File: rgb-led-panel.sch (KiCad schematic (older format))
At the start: 4 parts

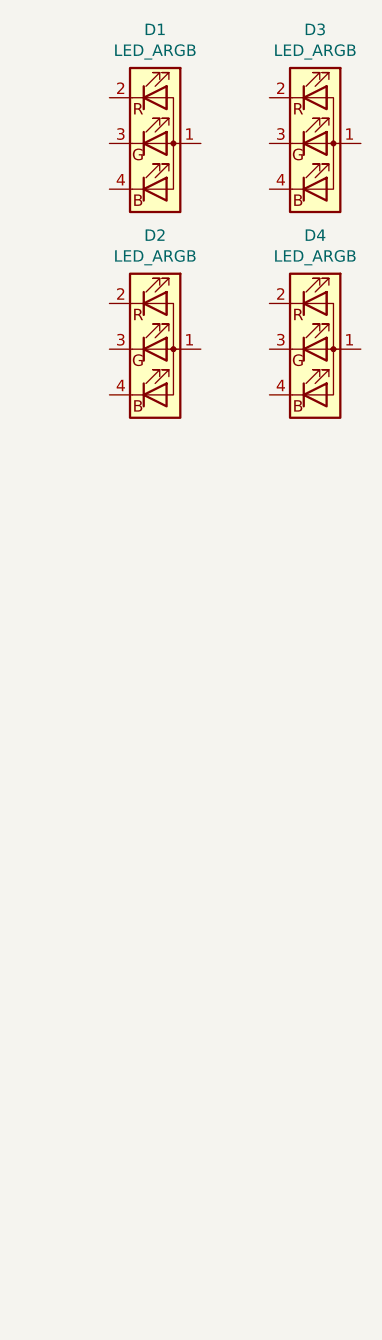
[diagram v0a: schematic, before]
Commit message: Layout 16x16 RGB panel
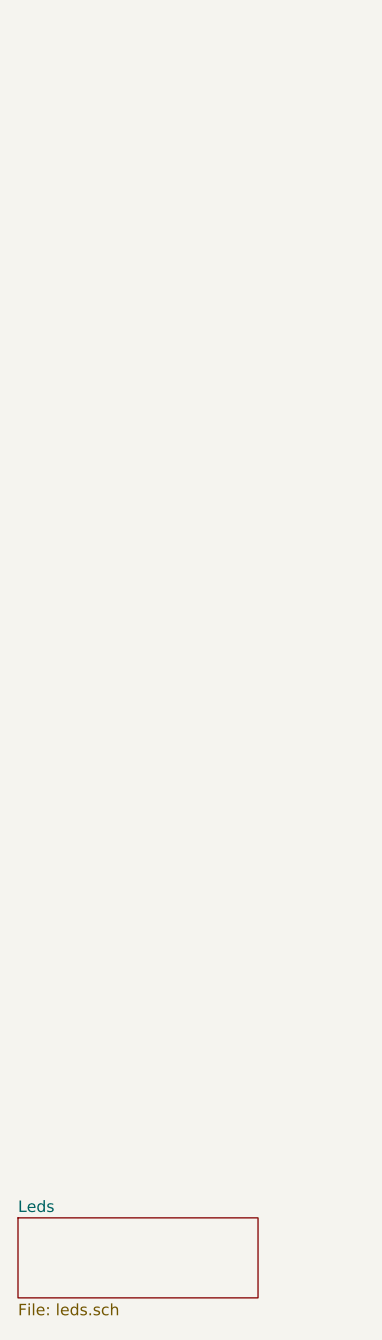
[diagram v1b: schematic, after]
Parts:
- removed D1, D2, D3, D4: LED_ARGB, LED_SMD_RGB:MHPA0808RGBDT, symbol Device:LED_ARGB
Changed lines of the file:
@@
 $Descr A4 11693 8268
 encoding utf-8
-Sheet 1 1
+Sheet 1 18
 Title ""
 Date ""
@@
 Comment4 ""
 $EndDescr
-$Comp
-L Device:LED_ARGB D1
-U 1 1 60A05D76
-P 3800 2950
-F 0 "D1" H 3800 3447 50  0000 C CNN
-F 1 "LED_ARGB" H 3800 3356 50  0000 C CNN
-F 2 "LED_SMD_RGB:MHPA0808RGBDT" H 3800 2900 50  0001 C CNN
-F 3 "~" H 3800 2900 50  0001 C CNN
-F 4 "C404279" H 3800 2950 50  0001 C CNN "LCSC"
-	1    3800 2950
-	1    0    0    -1
-$EndComp
-$Comp
-L Device:LED_ARGB D3
-U 1 1 60A06C39
-P 4500 2950
-F 0 "D3" H 4500 3447 50  0000 C CNN
-F 1 "LED_ARGB" H 4500 3356 50  0000 C CNN
-F 2 "LED_SMD_RGB:MHPA0808RGBDT" H 4500 2900 50  0001 C CNN
-F 3 "~" H 4500 2900 50  0001 C CNN
-F 4 "C404279" H 4500 2950 50  0001 C CNN "LCSC"
-	1    4500 2950
-	1    0    0    -1
-$EndComp
-$Comp
-L Device:LED_ARGB D2
-U 1 1 60A076CD
-P 3800 3850
-F 0 "D2" H 3800 4347 50  0000 C CNN
-F 1 "LED_ARGB" H 3800 4256 50  0000 C CNN
-F 2 "LED_SMD_RGB:MHPA0808RGBDT" H 3800 3800 50  0001 C CNN
-F 3 "~" H 3800 3800 50  0001 C CNN
-F 4 "C404279" H 3800 3850 50  0001 C CNN "LCSC"
-	1    3800 3850
-	1    0    0    -1
-$EndComp
-$Comp
-L Device:LED_ARGB D4
-U 1 1 60A07EC9
-P 4500 3850
-F 0 "D4" H 4500 4347 50  0000 C CNN
-F 1 "LED_ARGB" H 4500 4256 50  0000 C CNN
-F 2 "LED_SMD_RGB:MHPA0808RGBDT" H 4500 3800 50  0001 C CNN
-F 3 "~" H 4500 3800 50  0001 C CNN
-F 4 "C404279" H 4500 3850 50  0001 C CNN "LCSC"
-	1    4500 3850
-	1    0    0    -1
-$EndComp
+$Sheet
+S 3200 7650 1050 350
+U 61A87A3F
+F0 "Leds" 50
+F1 "leds.sch" 50
+$EndSheet
 $EndSCHEMATC
